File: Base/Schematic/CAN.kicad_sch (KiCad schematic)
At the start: 1 part, among them U3 CA-IS3052CW

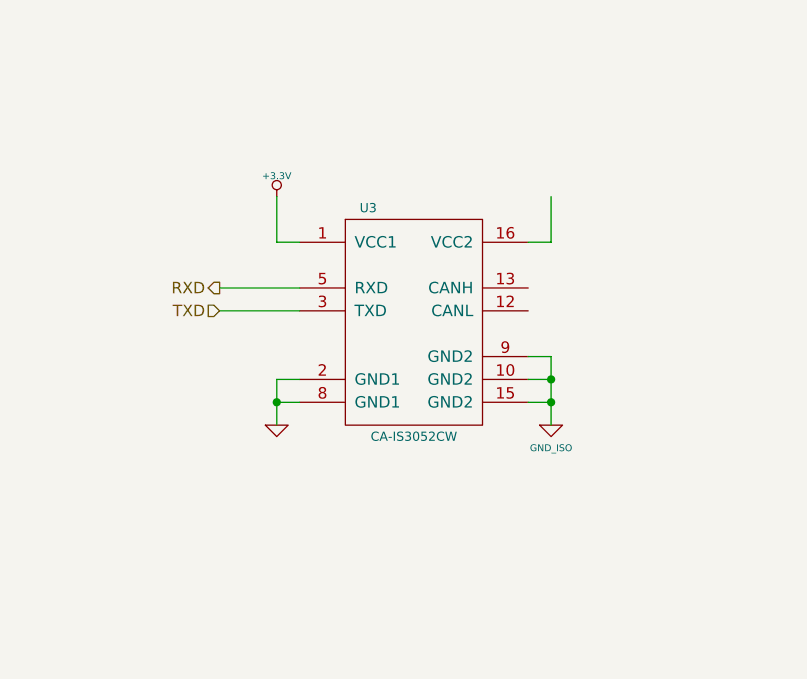
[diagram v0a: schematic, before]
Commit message: [Base 횔로도 업데이트] - CAN 통신용 5V 절연된 전원 추가
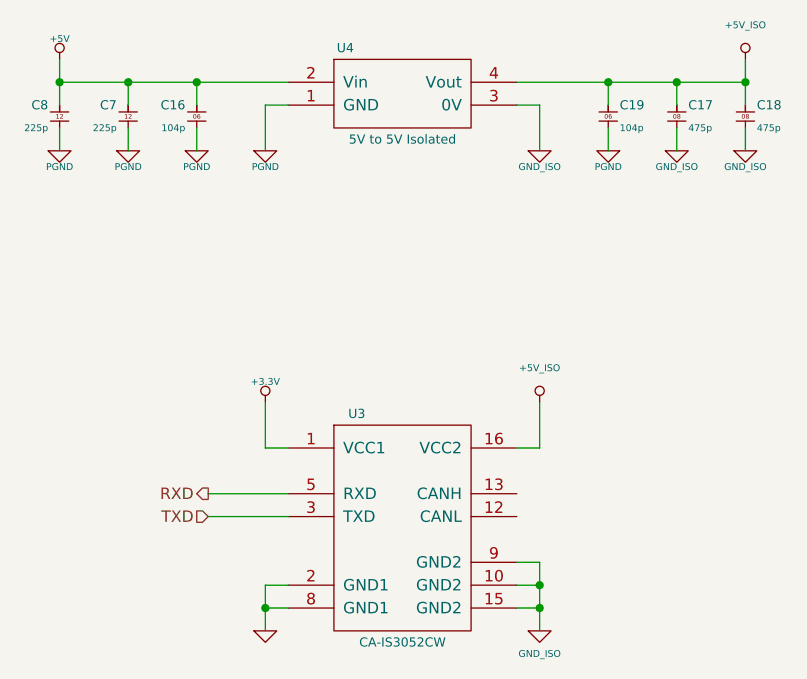
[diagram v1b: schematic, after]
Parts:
- added C16, C19: 0603B104K500, SMC:0603, symbol Capacitor_MLCC:0603B104K500
- added C17, C18: 0805B475K160, SMC:0805, symbol Capacitor_MLCC:0805B475K160
- added C7, C8: 1206B225K500, SMC:0805, symbol Capacitor_MLCC:1206B225K500
- added U4: B0505S-1W, ReSine PS:BXXS-1W, symbol Power_Module:B0505S-1W_ReSine PS
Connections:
- net GND_ISO: now also C17.1, C18.1, U4.3 (0V)
- net +5V_ISO: now reaches U3.16 (VCC2)
- net +5V_ISO: now also C17.2, C18.2, C19.2, U4.4 (Vout)
- new net +5V: C16.2, C7.2, C8.2, U4.2 (Vin)
- new net PGND: C16.1, C19.1, C7.1, C8.1, U4.1 (GND)
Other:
- moved on the sheet: U3
